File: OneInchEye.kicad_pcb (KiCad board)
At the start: 4 copper layers, 44.3 x 39 mm, 84 parts, among them J1 FH12A-22S-0.5SH(55), J2 QWIIC_CONNECTORJS-1MM, Q1 DMN3067LW, Q2 DMN3067LW, U1 LP5907MFX-1.8, U2 LP5907MFX-2.9, U3 IMX283EQJC, U4 TMP117AIDRVR, U5 ECS-2520MV-240-DN-TR, U6 AP3418KTR-G1

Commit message: Update to v1.4
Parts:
- removed Q1, Q2: DMN3067LW, Package_TO_SOT_SMD:SOT-23
- added C39: 100nF, Capacitor_SMD:C_0402_1005Metric, F.Cu at (144.6, 117.2)
- added C40: 100nF, Capacitor_SMD:C_0402_1005Metric, F.Cu at (138.6, 116.9)
- added C41: 100nF, Capacitor_SMD:C_0402_1005Metric, F.Cu at (151.0, 117.5)
- added FB4: BLM18KG102SN1D, Inductor_SMD:L_0402_1005Metric, F.Cu at (143.9, 114.6)
- added JP1: Jumper_3_Open, Jumper:SolderJumper-3_P1.3mm_Open_RoundedPad1.0x1.5mm_NumberLabels, F.Cu at (137.9, 87.5)
- added JP2: SolderJumper_2_Open, Jumper:SolderJumper-2_P1.3mm_Open_RoundedPad1.0x1.5mm, F.Cu at (159.9, 92.9)
- added R9: 10K, Resistor_SMD:R_0402_1005Metric, F.Cu at (135.9, 88.4)
- added U7: TCA9406DC, footprints:TCA9406DCUR, F.Cu at (141.7, 117.0)
- added U8: ATECC608A-MAHDA, Package_DFN_QFN:DFN-8-1EP_3x2mm_P0.5mm_EP1.3x1.5mm, F.Cu at (152.2, 120.4)
- moved C35 9.95 mm to (143.9, 112.7)
- moved U4 9.81 mm to (145.8, 113.0)
- moved C2 7.17 mm to (146.4, 105.6), turned to -90 degrees
- moved TP9 7.09 mm to (135.7, 94.4)
- moved TP11 7.00 mm to (156.8, 93.4)
- moved TP7 6.99 mm to (156.8, 91.2)
- moved R6 6.11 mm to (138.4, 91.7)
- moved R7 6.11 mm to (138.4, 90.5)
- moved C8 6.03 mm to (144.6, 106.8)
- moved C1 6.02 mm to (136.4, 96.9)
- moved C10 6.02 mm to (142.4, 100.1)
- moved C11 6.02 mm to (140.9, 110.6)
- moved C12 6.02 mm to (144.7, 101.8)
- moved C13 6.02 mm to (132.7, 99.3)
- moved C14 6.02 mm to (143.9, 110.6)
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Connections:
- C35 pad 2: +1V8 -> Net-(C35-Pad2)
- J1 pad 6: CAM_EN -> Net-(J1-Pad6)
- U4 pad 1: SCL_1V8 -> SCL_3V3
- U4 pad 5: +1V8 -> Net-(C35-Pad2)
- U4 pad 6: SDA_1V8 -> SDA_3V3
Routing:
- net +3V3: track 70.9 -> 100.4 mm, vias 0 -> 3
- net CAM_EN: track 61.7 -> 36.7 mm, vias 4 -> 5
- net Net-(J1-Pad6): track 0.00 -> 19.8 mm
- net SCL_3V3: track 30.3 -> 40.9 mm, vias 4 -> 2
- net +1V8: track 26.6 -> 18.3 mm, vias 12 -> 10
- net SDA_3V3: track 33.8 -> 40.5 mm, vias 0 -> 7
- net SCL_1V8: track 14.5 -> 10.5 mm
- net SDA_1V8: track 12.6 -> 9.30 mm
- net Net-(JP1-Pad2): track 0.00 -> 2.21 mm
- net RST_1V8: track 18.1 -> 15.9 mm
- net Net-(C35-Pad2): track 0.00 -> 1.94 mm
- net +2V9: track 3.86 -> 2.74 mm
- net +1V2: track 15.1 -> 14.2 mm
- net GND: vias 84 -> 104
- added copper zone on B.Cu, net +1V2
- added copper zone on B.Cu, net +1V8
- added copper zone on B.Cu, net +2V9
- added copper zone on F.Cu, net +3V3
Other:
- outline, holes or cut-outs redrawn
- board text added: "Designed By Will Whang 2023/10/25"
- board text added: "OneInchEye V1.4"
- board text removed: "Designed By Will Whang 2023/02/17"
- board text removed: "OneInchEye V1.3"
- board text removed: "{ "ViaStitching": "0.1", "stitch_zone_0": { "HSpacing": "0.5", "VSpacing": "0.5", "Clearance": "0", "Randomize": false } }"
- board text removed: "{ "ViaStitching": "0.1", "stitch_zone_0": { "HSpacing": "1", "VSpacing": "1", "Clearance": "0", "Randomize": false } }"

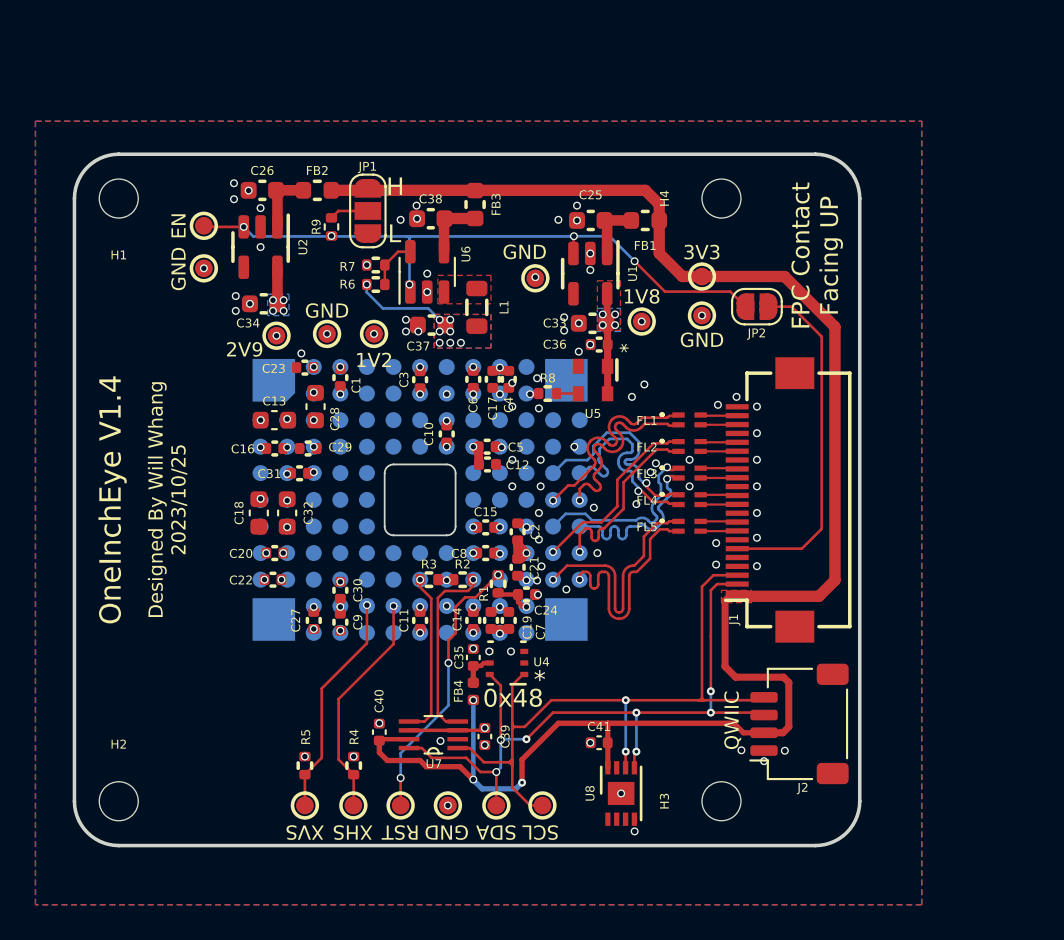
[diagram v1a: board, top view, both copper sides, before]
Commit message: Adding IMU and update board outline to 39mm square
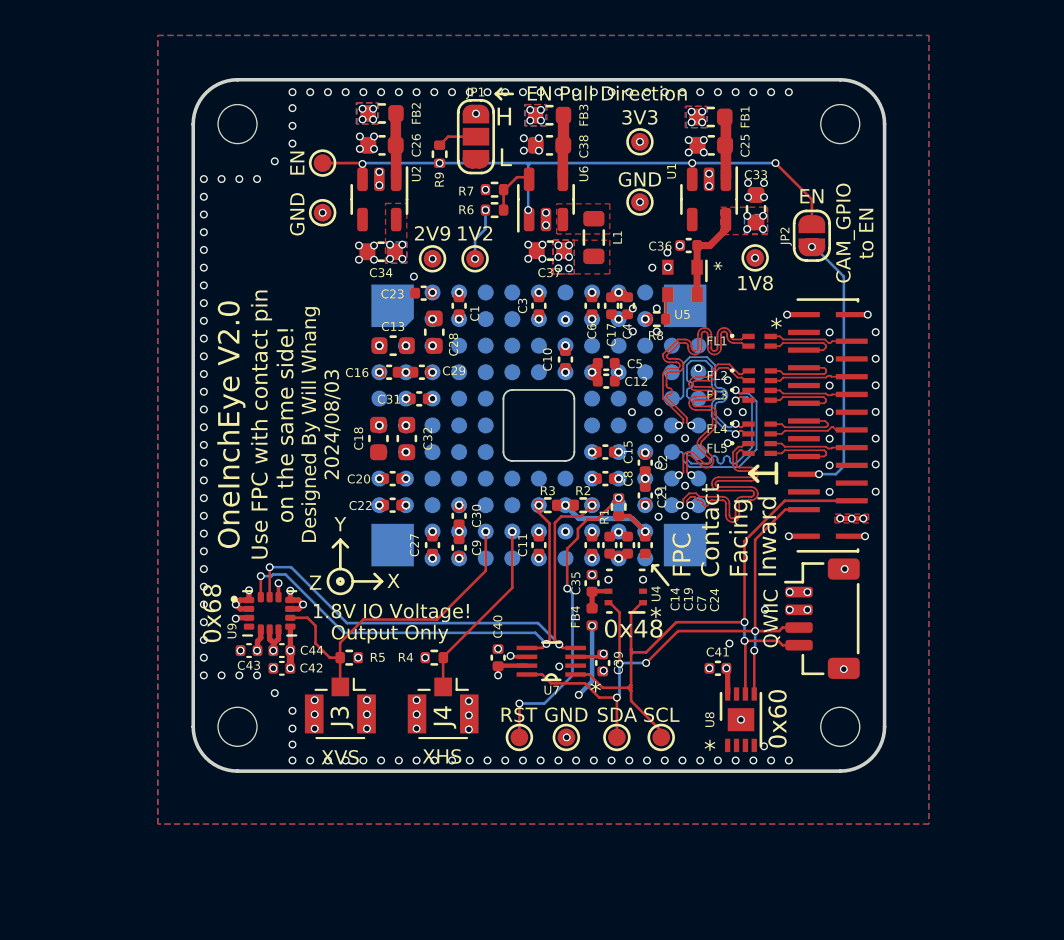
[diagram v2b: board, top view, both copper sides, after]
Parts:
- removed TP11, TP2, TP3, TP9: TestPoint, TestPoint:TestPoint_Pad_D1.0mm
- added C42: 100n, Capacitor_SMD:C_0402_1005Metric, F.Cu at (133.1, 113.3)
- added C43: 10nF, Capacitor_SMD:C_0402_1005Metric, F.Cu at (131.2, 112.3)
- added C44: 2.2uF, Capacitor_SMD:C_0402_1005Metric, F.Cu at (133.1, 112.3)
- added J3: Conn_Coaxial, Connector_Coaxial:U.FL_Hirose_U.FL-R-SMT-1_Vertical, F.Cu at (136.4, 115.4)
- added J4: Conn_Coaxial, Connector_Coaxial:U.FL_Hirose_U.FL-R-SMT-1_Vertical, F.Cu at (142.2, 115.4)
- added JPR1: 0R, Resistor_SMD:R_0402_1005Metric, F.Cu at (144.1, 83.9)
- added JPR2: 0R, Resistor_SMD:R_0402_1005Metric, F.Cu at (163.0, 88.9)
- added U9: ICM-42688-P, footprints:PQFN50P300X250X97-14N, F.Cu at (132.4, 110.2)
- FL1, FL2, FL3, FL4, FL5: value DLP11SN900HL2L -> KCZ1210AH900HRTD25
- J1: value FH12A-22S-0.5SH(55) -> Conn_01x22_Shielded; footprint Connector_FFC-FPC:Hirose_FH12-22S-0.5SH_1x22-1MP_P0.50mm_Horizontal -> footprints:TF3822S05SV830
- J2: value QWIIC_CONNECTORJS-1MM -> Conn_01x04_Shielded; footprint Connector_JST:JST_SH_SM04B-SRSS-TB_1x04-1MP_P1.00mm_Horizontal -> Connector_JST:JST_SH_BM04B-SRSS-TB_1x04-1MP_P1.00mm_Vertical
- R2, R3: value 10K -> DNP
- U5: value ECS-2520MV-240-DN-TR -> ECS-2520S18-240-FN-TR
- moved C33 11.3 mm to (159.8, 87.4), turned to 90 degrees
- moved TP6 9.81 mm to (141.6, 90.2)
- moved TP7 8.37 mm to (153.3, 83.6)
- moved C21 8.26 mm to (153.6, 103.5)
- moved C5 8.20 mm to (151.4, 96.1)
- moved C2 8.19 mm to (153.6, 101.7)
- moved C12 8.18 mm to (151.4, 97.1)
- moved R1 8.07 mm to (152.1, 104.2)
- moved C25 8.01 mm to (157.3, 83.8)
- moved R2 7.99 mm to (150.1, 104.1)
- moved C15 7.98 mm to (151.3, 101.1)
- moved C22 7.95 mm to (139.3, 104.1)
- moved C31 7.95 mm to (140.8, 98.1)
- moved C8 7.95 mm to (151.3, 102.6)
- moved C18 7.95 mm to (138.6, 100.3)
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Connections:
- net Net-(FL1-Pad2) renamed /D0_N
- net Net-(FL1-Pad3) renamed /D0_P
- net Net-(FL2-Pad2) renamed /D1_N
- net Net-(FL2-Pad3) renamed /D1_P
- net Net-(FL3-Pad2) renamed /CLK_N
- net Net-(FL3-Pad3) renamed /CLK_P
- net Net-(FL4-Pad2) renamed /D2_N
- net Net-(FL4-Pad3) renamed /D2_P
- net Net-(FL5-Pad2) renamed /D3_N
- net Net-(FL5-Pad3) renamed /D3_P
- J1 pad MP: (no net) -> GND
- J2 pad MP: (no net) -> GND
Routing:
- net +3V3: track 100.4 -> 7.84 mm, vias 3 -> 23
- net SCL_1V8: track 10.5 -> 30.3 mm, vias 1 -> 3
- net SDA_1V8: track 9.30 -> 28.3 mm, vias 1 -> 3
- net GND: track 0.00 -> 8.72 mm, vias 104 -> 235
- net XVS: track 12.8 -> 18.9 mm
- net CAM_D1_N: track 10.6 -> 16.0 mm
- net CAM_D1_P: track 10.6 -> 15.7 mm
- net +1V2: track 14.2 -> 9.21 mm, vias 22 -> 21
- net SDA_3V3: track 40.5 -> 36.2 mm, vias 7 -> 5
- net Net-(J1-Pad6): track 19.8 -> 15.6 mm, vias 0 -> 2
- net CAM_D0_P: track 12.0 -> 15.5 mm
- net CAM_D0_N: track 12.0 -> 15.5 mm
- net /D0_N: track 2.08 -> 4.78 mm
- net /D2_N: track 2.08 -> 4.75 mm
- net /CLK_N: track 2.08 -> 4.71 mm
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- added copper zone on F.Cu, net +2V9
- added copper zone on B.Cu, net +3V3
- added copper zone on In2.Cu, net +3V3
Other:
- board size 44.3 x 39 mm -> 39 x 39 mm
- board text added: "0x60"
- board text added: "0x68"
- board text added: "1.8V IO Voltage!"
- board text added: "CAM_GPIO to EN"
- board text added: "Designed By Will Whang 2024/08/03"
- board text added: "EN Pull Direction"
- board text added: "FPC Contact Facing Inward"
- board text added: "Notes: VIA in PAD PCB process"
- board text added: "OneInchEye V2.0"
- board text added: "Output Only"
- board text added: "Use FPC with contact pin on the same side!"
- board text added: "X"
- board text added: "Y"
- board text added: "Z"
- board text removed: "Designed By Will Whang 2023/10/25"
- board text removed: "FPC Contact Facing UP"
- board text removed: "OneInchEye V1.4"

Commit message: V2.1
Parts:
- removed C41: 100nF, Capacitor_SMD:C_0402_1005Metric
- removed JP1: Jumper_3_Open, Jumper:SolderJumper-3_P1.3mm_Open_RoundedPad1.0x1.5mm_NumberLabels
- removed JP2: SolderJumper_2_Open, Jumper:SolderJumper-2_P1.3mm_Open_RoundedPad1.0x1.5mm
- removed JPR1, JPR2: 0R, Resistor_SMD:R_0402_1005Metric
- removed TP10: TestPoint, TestPoint:TestPoint_Pad_D1.0mm
- removed U8: ATECC608A-MAHDA, Package_DFN_QFN:DFN-8-1EP_3x2mm_P0.5mm_EP1.3x1.5mm
- added ?: , clipboard:33f3fa26-f2d6-4a6c-90fd-caa01b2fdac3, F.Cu at (133.2, 85.8)
- added C45: 1uF, Capacitor_SMD:C_0402_1005Metric, F.Cu at (138.5, 85.0)
- added C46: 10nF, Capacitor_SMD:C_0402_1005Metric, F.Cu at (137.5, 91.7)
- added C47: 10uF, Capacitor_SMD:C_0603_1608Metric, F.Cu at (135.8, 89.0)
- added R10: 3.01K, Resistor_SMD:R_0402_1005Metric, F.Cu at (136.5, 91.7)
- added R11: 1.15K, Resistor_SMD:R_0402_1005Metric, F.Cu at (138.5, 91.7)
- C26: value 4.7uF -> NFM18CC101R1C3D; footprint Capacitor_SMD:C_0603_1608Metric -> footprints:NFM18CC101R1C3D
- C34: value 4.7uF -> 10uF
- U2: value LP5907MFX-2.9 -> TPS7A90; footprint Package_TO_SOT_SMD:SOT-23-5 -> Package_DFN_QFN:Texas_S-PDSO-N10_EP1.2x2mm
- U9: footprint footprints:PQFN50P300X250X97-14N -> footprints:IIM42352
- moved R9 13.0 mm to (155.0, 85.2)
- moved TP15 9.60 mm to (145.0, 84.8)
- moved C34 5.01 mm to (136.5, 85.3)
- moved C26 1.66 mm to (137.2, 83.1), turned to -90 degrees
- moved U2 1.33 mm to (138.2, 88.1), turned to 90 degrees
- moved FB2 0.76 mm to (139.5, 82.1), turned to 180 degrees
- moved TP4 0.45 mm to (144.0, 89.8)
- moved TP6 0.45 mm to (141.6, 89.8)
- moved C33 0.09 mm to (159.8, 87.3)
- moved C37 0.06 mm to (148.2, 89.7)
- moved C28 0.06 mm to (141.7, 94.4)
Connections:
- C26 pad 1: GND -> Net-(C26-Pad1)
- C26 pad 2: Net-(C26-Pad2) -> GND
- C34 pad 1: +2V9 -> Net-(U2-SS_CTRL)
- FB2 pad 2: Net-(C26-Pad2) -> Net-(C26-Pad1)
- J1 pad 6: Net-(J1-Pad6) -> CAM_EN
- R9 pad 2: Net-(JP1-Pad2) -> GND
- U2 pad 1: Net-(C26-Pad2) -> +2V9
- U2 pad 2: GND -> +2V9
- U2 pad 3: CAM_EN -> Net-(U2-FB)
- U2 pad 4: unconnected-(U2-Pad4) -> GND
- U2 pad 5: +2V9 -> unconnected-(U2-PG-Pad5)
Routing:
- net Net-(J1-Pad6): track 15.6 -> 0.00 mm, vias 2 -> 0
- net CAM_EN: track 34.4 -> 49.5 mm
- net Net-(U2-FB): track 0.00 -> 4.44 mm
- net Net-(U2-SS_CTRL): track 0.00 -> 3.78 mm, vias 0 -> 2
- net Net-(C26-Pad2): track 3.63 -> 0.00 mm
- net SDA_3V3: track 36.2 -> 33.2 mm, vias 5 -> 3
- net SCL_3V3: track 38.5 -> 35.6 mm
- net Net-(JP1-Pad2): track 2.25 -> 0.00 mm
- net Net-(U2-NR/SS): track 0.00 -> 1.62 mm
- net +3V3: track 7.84 -> 6.54 mm, vias 23 -> 21
- net +2V9: track 0.14 -> 0.08 mm, vias 13 -> 17
- net GND: vias 235 -> 419
- added copper zone on F.Cu, net Net-(C26-Pad1)
- added copper zone on F.Cu, net Net-(U2-SS_CTRL)
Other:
- board text added: "Cam View"
- board text added: "Designed By Will Whang 2025/07/27"
- board text added: "Github"
- board text added: "OneInchEye V2.1"
- board text removed: "0x60"
- board text removed: "CAM_GPIO to EN"
- board text removed: "Designed By Will Whang 2024/08/03"
- board text removed: "EN Pull Direction"
- board text removed: "OneInchEye V2.0"
